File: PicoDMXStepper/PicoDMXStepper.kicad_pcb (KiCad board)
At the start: 2 copper layers, 58.3 x 71.2 mm, 27 parts, among them J1 Pwr In, J2 DMX Serial, J3 Stepper Out, J4 Limit SW, SW2 SW_DIP_x04, U1 AMS1117-5.0, U2 Pico, U3 SP3485EN

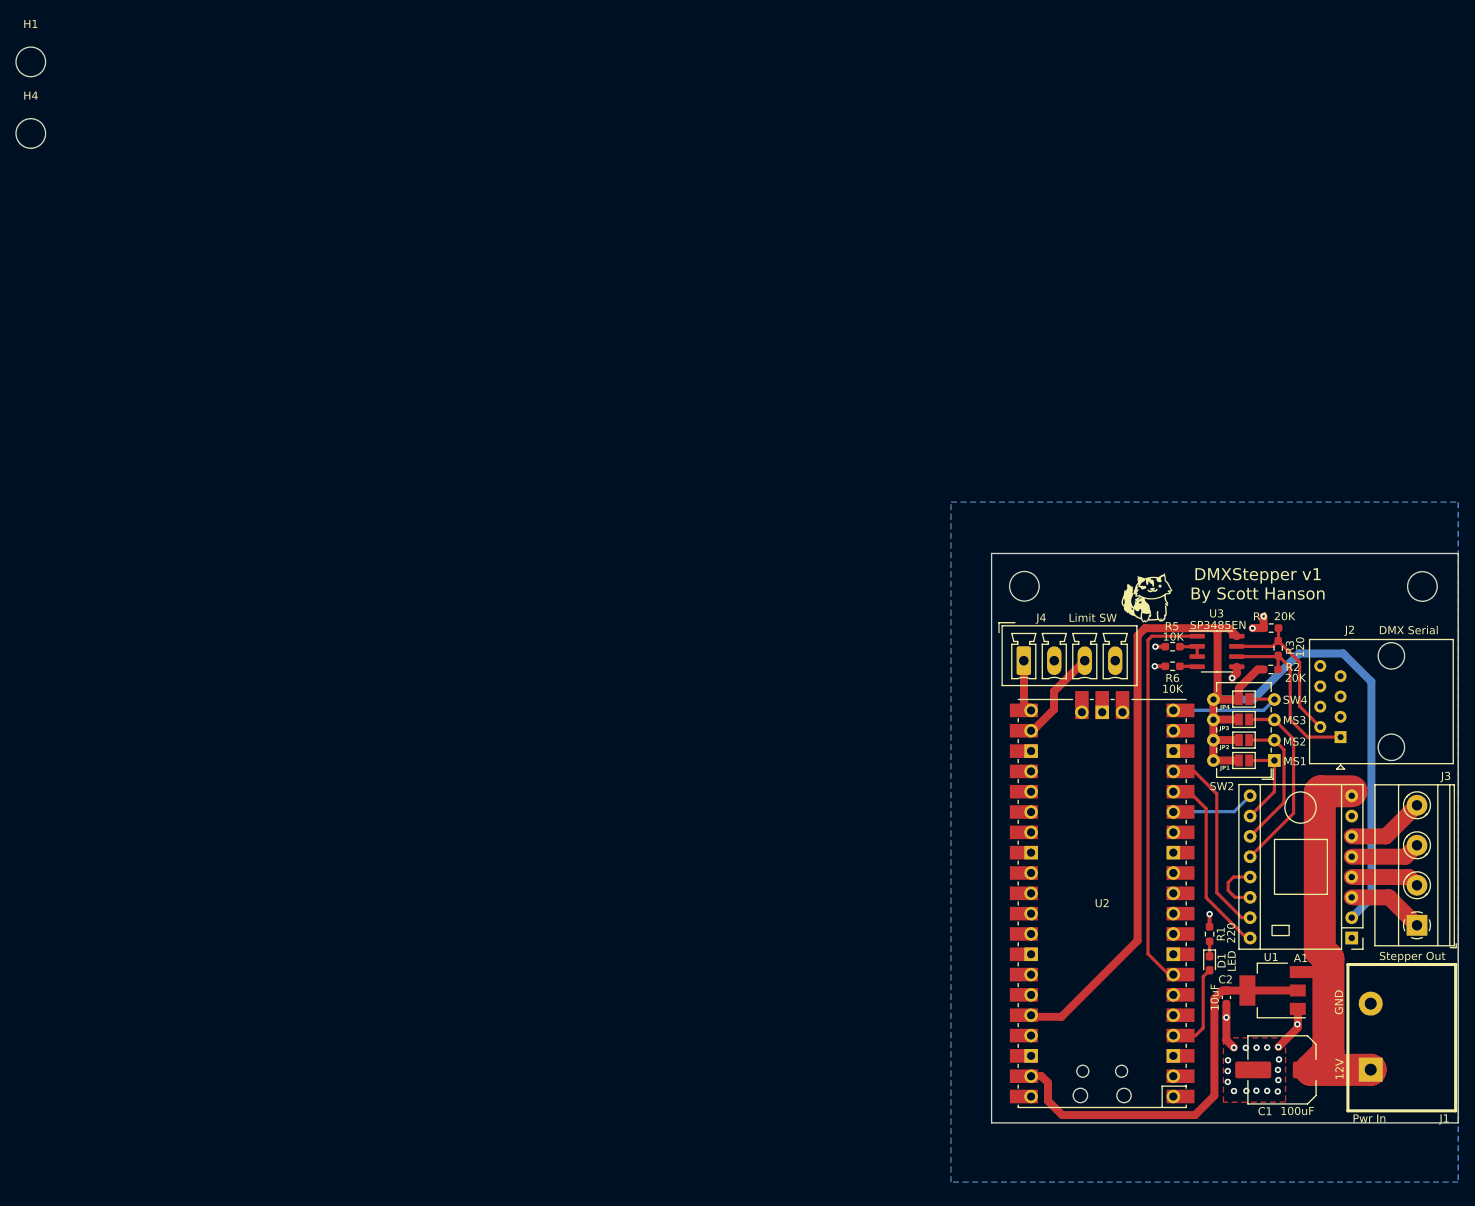
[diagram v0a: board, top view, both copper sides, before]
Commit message: redo PCB layout, Add servo headers and opocouplers to limit switches
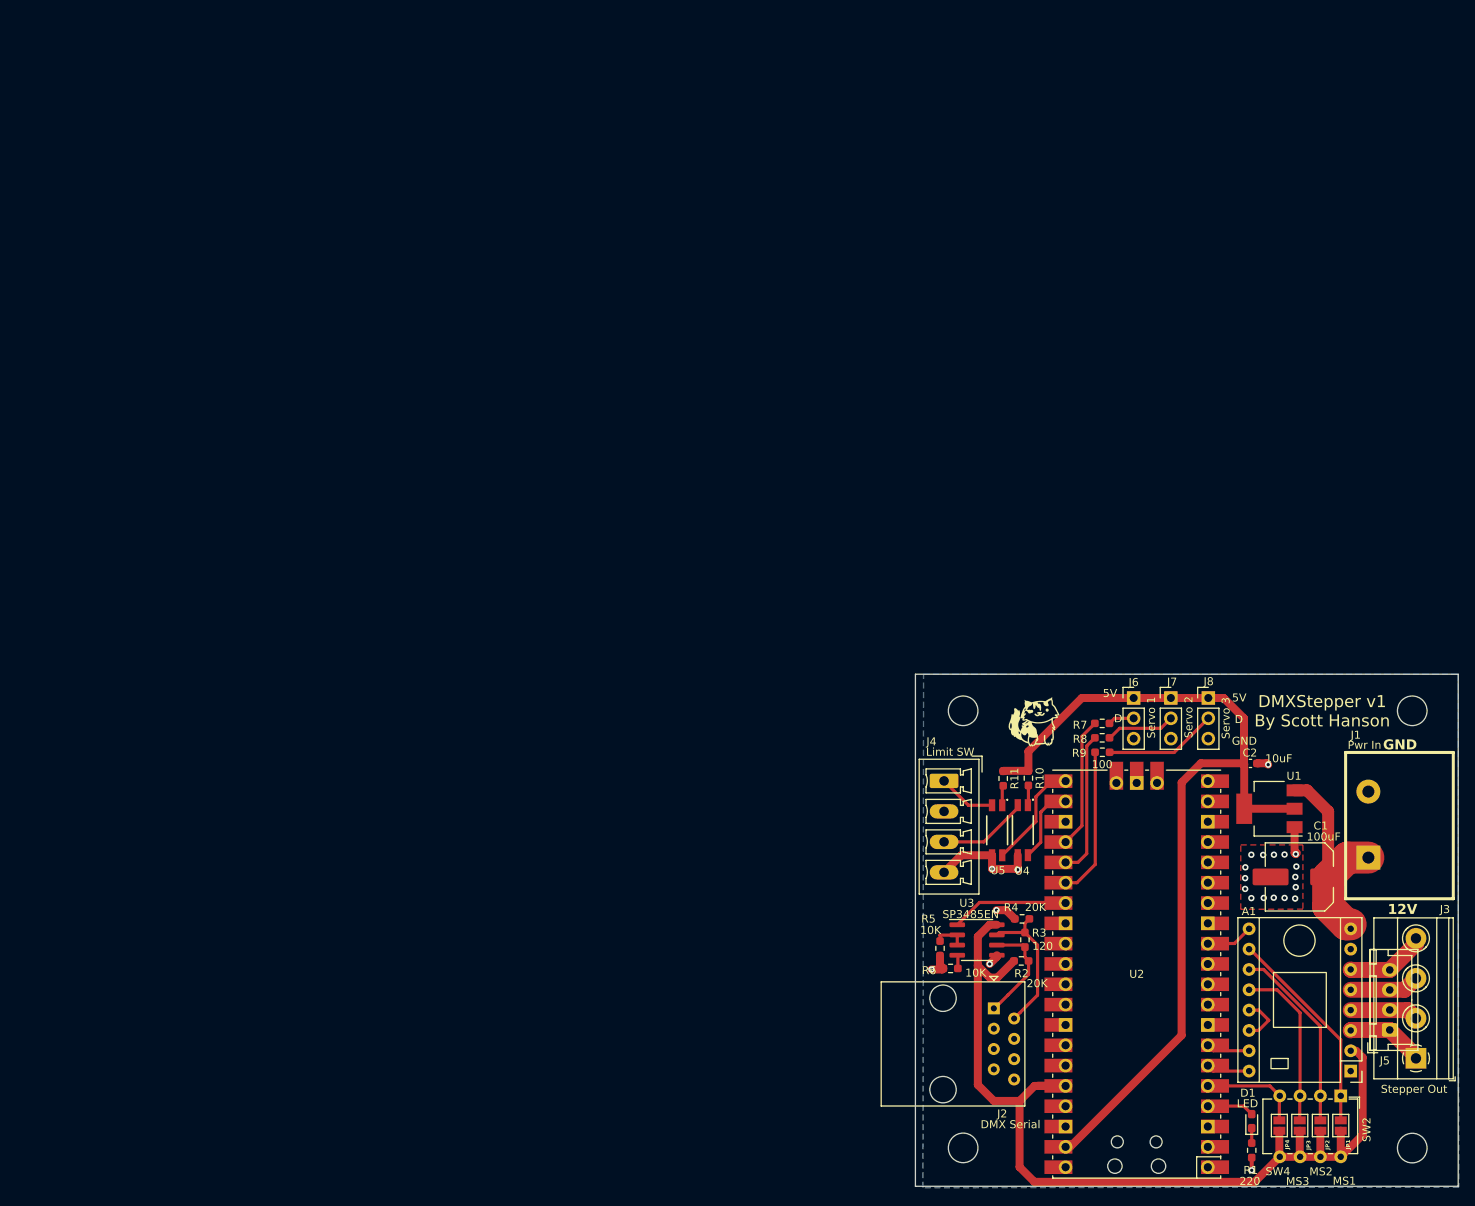
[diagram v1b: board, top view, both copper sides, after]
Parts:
- added J5: Stepper Out 2, Connector_JST:JST_XH_B4B-XH-A_1x04_P2.50mm_Vertical, F.Cu at (173.8, 125.0)
- added J6: Servo 1, Connector_PinHeader_2.54mm:PinHeader_1x03_P2.54mm_Vertical, F.Cu at (141.8, 83.5)
- added J7: Servo 2, Connector_PinHeader_2.54mm:PinHeader_1x03_P2.54mm_Vertical, F.Cu at (146.5, 83.5)
- added J8: Servo 3, Connector_PinHeader_2.54mm:PinHeader_1x03_P2.54mm_Vertical, F.Cu at (151.2, 83.5)
- added R10: 220, Resistor_SMD:R_0603_1608Metric_Pad0.98x0.95mm_HandSolder, F.Cu at (128.7, 93.5)
- added R11: 220, Resistor_SMD:R_0603_1608Metric_Pad0.98x0.95mm_HandSolder, F.Cu at (125.5, 93.6)
- added R7: 100, Resistor_SMD:R_0603_1608Metric_Pad0.98x0.95mm_HandSolder, F.Cu at (137.9, 86.7)
- added R8: 100, Resistor_SMD:R_0603_1608Metric_Pad0.98x0.95mm_HandSolder, F.Cu at (137.9, 88.5)
- added R9: 100, Resistor_SMD:R_0603_1608Metric_Pad0.98x0.95mm_HandSolder, F.Cu at (137.9, 90.3)
- added U4: LTV-214G, PicoDMXStepper:LTV214, F.Cu at (128.0, 100.0)
- added U5: LTV-214G, PicoDMXStepper:LTV214, F.Cu at (124.8, 100.0)
- moved H4 214.3 mm to (176.7, 139.8)
- moved H1 178.9 mm to (120.5, 139.7)
- moved J2 55.0 mm to (124.4, 122.3), turned to -90 degrees
- moved JP4 53.5 mm to (160.0, 136.9), turned to 90 degrees
- moved JP3 51.2 mm to (162.6, 136.9), turned to 90 degrees
- moved JP2 49.1 mm to (165.2, 136.9), turned to 90 degrees
- moved R3 48.3 mm to (128.2, 113.7)
- moved R2 48.0 mm to (127.8, 116.4)
- moved R4 47.9 mm to (127.9, 111.1)
- moved R5 47.6 mm to (117.6, 114.8), turned to -90 degrees
- moved JP1 47.2 mm to (167.7, 136.9), turned to 90 degrees
- moved U3 46.9 mm to (122.3, 113.7)
- moved R6 46.9 mm to (118.9, 117.3)
- moved SW2 42.7 mm to (167.7, 133.2), turned to -90 degrees
- moved C2 29.4 mm to (156.4, 91.7), turned to 0 degrees
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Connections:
- net /1A renamed 1A
- net /1B renamed 1B
- net /2A renamed 2A
- net /2B renamed 2B
- U2 pad 12: unconnected-(U2-GPIO9-Pad12) -> EN
- U2 pad 15: EN -> unconnected-(U2-GPIO11-Pad15)
- U2 pad 16: DIR -> unconnected-(U2-GPIO12-Pad16)
- U2 pad 17: STEP -> unconnected-(U2-GPIO13-Pad17)
- U2 pad 20: SW4 -> unconnected-(U2-GPIO15-Pad20)
- U2 pad 21: Net-(J4-Pin_1) -> Net-(U2-GPIO16)
- U2 pad 22: Net-(J4-Pin_3) -> Net-(U2-GPIO17)
- U2 pad 24: unconnected-(U2-GPIO18-Pad24) -> SEV1
- U2 pad 25: unconnected-(U2-GPIO19-Pad25) -> SEV2
- U2 pad 26: unconnected-(U2-GPIO20-Pad26) -> SEV3
- U2 pad 27: unconnected-(U2-GPIO21-Pad27) -> DMX_OUT
- U2 pad 5: unconnected-(U2-GPIO3-Pad5) -> SW4
- U2 pad 6: unconnected-(U2-GPIO4-Pad6) -> DIR
- U2 pad 7: DMX_OUT -> STEP
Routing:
- net +5V: track 50.3 -> 114.7 mm
- net +3V3: track 157.8 -> 122.6 mm
- net DMX_OUT: track 49.8 -> 14.7 mm
- net +12V: track 52.1 -> 26.9 mm
- net STEP: track 24.4 -> 5.44 mm
- net SEV3: track 0.00 -> 18.7 mm
- net DIR: track 23.7 -> 5.44 mm
- net SEV2: track 0.00 -> 18.0 mm
- net SEV1: track 0.00 -> 16.3 mm
- net MS1: track 11.4 -> 26.2 mm
- net Net-(J8-Pin_2): track 0.00 -> 14.1 mm
- net Net-(U2-GPIO16): track 0.00 -> 13.6 mm
- net Net-(U2-GPIO17): track 0.00 -> 9.69 mm
- net Net-(U3-A): track 22.8 -> 13.3 mm
- net Net-(J7-Pin_2): track 0.00 -> 8.68 mm
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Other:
- board size 58.3 x 71.2 mm -> 67.8 x 64 mm
- board text added: "5V"
- board text added: "D"

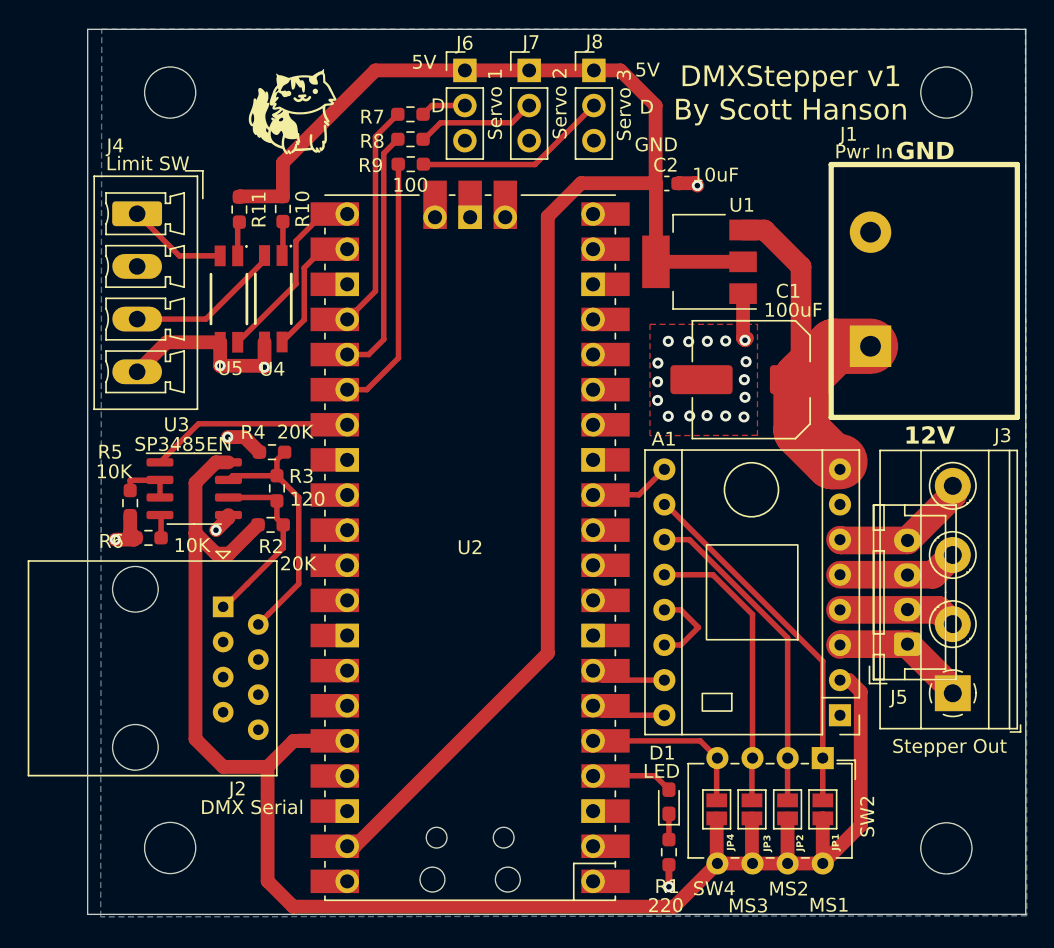
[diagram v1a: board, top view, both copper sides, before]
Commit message: added Optocoupler to limits switches
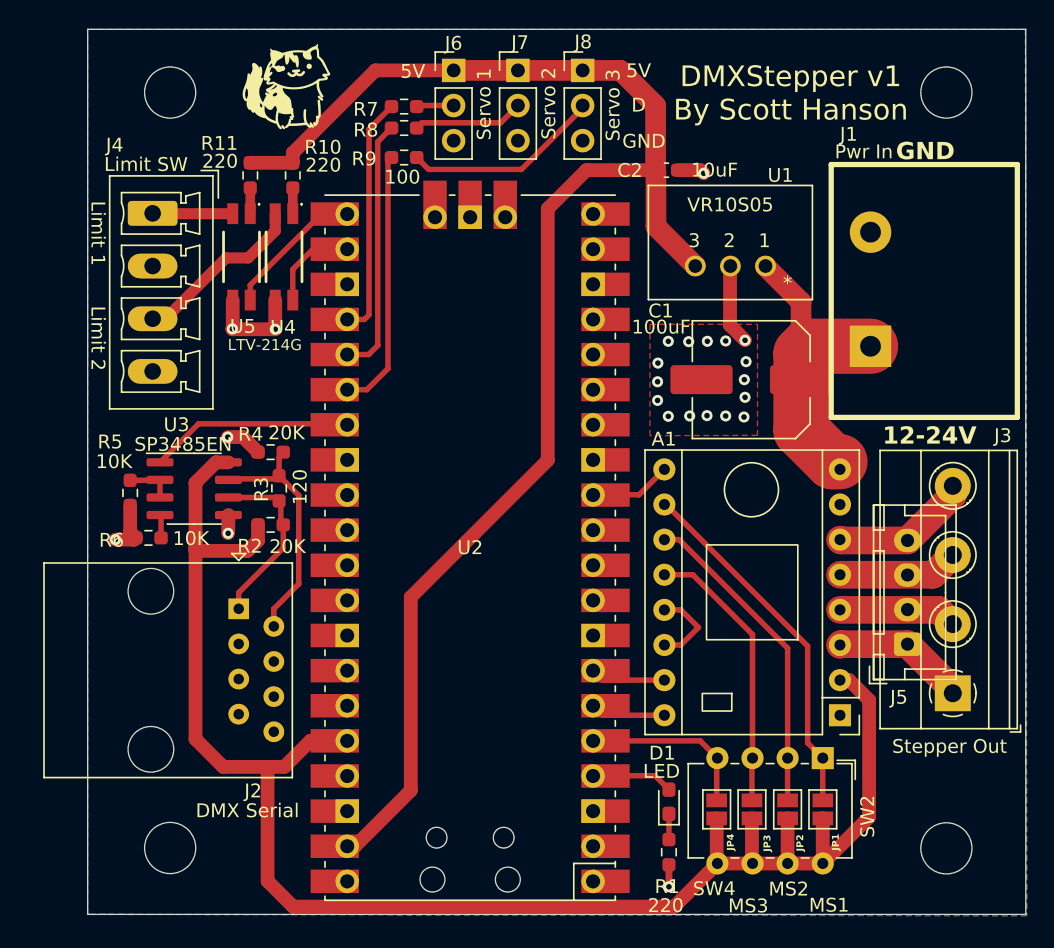
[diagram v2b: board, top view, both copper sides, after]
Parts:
- U1: value AMS1117-5.0 -> VR10S05; footprint Package_TO_SOT_SMD:SOT-223-3_TabPin2 -> PicoDMXStepper:VR10S05
- moved U1 4.78 mm to (163.6, 97.6)
- moved U5 3.18 mm to (125.7, 97.0)
- moved U4 3.13 mm to (128.8, 97.0)
- moved R11 2.59 mm to (126.3, 91.1)
- moved R10 2.53 mm to (129.4, 91.1)
- moved G*** 1.86 mm to (128.8, 83.9)
- moved J2 1.13 mm to (125.5, 122.4)
- moved J4 1.12 mm to (119.3, 93.8)
- moved C2 0.97 mm to (156.4, 90.7)
- moved R8 0.93 mm to (137.4, 87.7)
- moved J8 0.81 mm to (150.4, 83.5)
- moved J6 0.81 mm to (141.0, 83.5)
- moved J7 0.81 mm to (145.7, 83.5)
- moved R5 0.74 mm to (117.6, 114.0)
- moved R7 0.72 mm to (137.4, 86.1)
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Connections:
- U1 pad 1: GND -> +12V
- U1 pad 2: +5V -> GND
- U1 pad 3: +12V -> +5V
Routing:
- net +5V: track 114.7 -> 107.7 mm
- net Net-(U2-GPIO16): track 13.6 -> 10.2 mm
- net GND: track 27.8 -> 24.6 mm
- net +12V: track 26.9 -> 23.8 mm
- net Net-(U2-GPIO17): track 9.69 -> 6.77 mm
- net +3V3: track 122.6 -> 120.8 mm
- net Net-(J4-Pin_1): track 7.26 -> 5.80 mm
- net Net-(J4-Pin_3): track 11.3 -> 12.7 mm
- net SEV1: track 16.3 -> 17.4 mm
- net MS3: track 21.0 -> 20.2 mm
- net Net-(U3-DE): track 4.18 -> 3.44 mm
- net Net-(J7-Pin_2): track 8.68 -> 7.99 mm
- net Net-(R11-Pad2): track 2.49 -> 1.86 mm
- net Net-(R10-Pad2): track 2.48 -> 1.86 mm
- net SEV2: track 18.0 -> 18.6 mm
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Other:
- board text added: "1"
- board text added: "12-24V"
- board text added: "2"
- board text added: "3"
- board text added: "Limit 1"
- board text added: "Limit 2"
- board text removed: "12V"
